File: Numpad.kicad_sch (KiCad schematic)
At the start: 102 parts, among them J1 USB_C_Receptacle_USB2.0, J3 AVR-ISP-6, Q101 DMN2041L, Q2 DMN2041L, SW10 SW_Push, SW11 SW_Push, SW12 SW_Push, SW13 SW_Push, SW14 SW_Push, SW15 SW_Push, SW16 SW_Push, SW17 SW_Push, SW18 SW_Push, SW19 SW_Push, SW2 SW_Push, SW21 SW_Push, SW3 SW_Push, SW4 SW_Push, SW5 SW_Push, SW6 SW_Push, SW7 SW_Push, SW8 SW_Push, SW9 SW_Push, U1 ATmega32U2-A, Y1 16MHz

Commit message: more routing
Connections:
- net D+: now also D1.3 (I/O2); no longer D1.2 (I/O1)
- net D-: now also D1.2 (I/O1); no longer D1.3 (I/O2)
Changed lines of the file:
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@@
   (junction (at 215.9 214.63) (diameter 0) (color 0 0 0 0)
   )
+  (junction (at 105.41 113.03) (diameter 0) (color 0 0 0 0)
+  )
   (junction (at 205.74 214.63) (diameter 0) (color 0 0 0 0)
   )
@@
   (junction (at 313.69 134.62) (diameter 0) (color 0 0 0 0)
   )
+  (junction (at 232.41 34.29) (diameter 0) (color 0 0 0 0)
+  )
+  (junction (at 182.88 196.85) (diameter 0) (color 0 0 0 0)
+  )
+  (junction (at 341.63 124.46) (diameter 0) (color 0 0 0 0)
+  )
+  (junction (at 177.8 93.98) (diameter 0) (color 0 0 0 0)
+  )
+  (junction (at 341.63 114.3) (diameter 0) (color 0 0 0 0)
+  )
+  (junction (at 195.58 229.87) (diameter 0) (color 0 0 0 0)
+  )
+  (junction (at 330.2 140.97) (diameter 0) (color 0 0 0 0)
+  )
+  (junction (at 215.9 229.87) (diameter 0) (color 0 0 0 0)
+  )
+  (junction (at 226.06 212.09) (diameter 0) (color 0 0 0 0)
+  )
+  (junction (at 205.74 212.09) (diameter 0) (color 0 0 0 0)
+  )
+  (junction (at 236.22 232.41) (diameter 0) (color 0 0 0 0)
+  )
+  (junction (at 185.42 196.85) (diameter 0) (color 0 0 0 0)
+  )
+  (junction (at 236.22 214.63) (diameter 0) (color 0 0 0 0)
+  )
+  (junction (at 242.57 34.29) (diameter 0) (color 0 0 0 0)
+  )
+  (junction (at 185.42 214.63) (diameter 0) (color 0 0 0 0)
+  )
+  (junction (at 355.6 139.7) (diameter 0) (color 0 0 0 0)
+  )
+  (junction (at 195.58 232.41) (diameter 0) (color 0 0 0 0)
+  )
+  (junction (at 344.17 130.81) (diameter 0) (color 0 0 0 0)
+  )
+  (junction (at 215.9 212.09) (diameter 0) (color 0 0 0 0)
+  )
+  (junction (at 316.23 130.81) (diameter 0) (color 0 0 0 0)
+  )
+  (junction (at 215.9 196.85) (diameter 0) (color 0 0 0 0)
+  )
+  (junction (at 345.44 151.13) (diameter 0) (color 0 0 0 0)
+  )
+  (junction (at 205.74 196.85) (diameter 0) (color 0 0 0 0)
+  )
+  (junction (at 226.06 214.63) (diameter 0) (color 0 0 0 0)
+  )
+  (junction (at 195.58 214.63) (diameter 0) (color 0 0 0 0)
+  )
+  (junction (at 237.49 34.29) (diameter 0) (color 0 0 0 0)
+  )
+  (junction (at 167.64 93.98) (diameter 0) (color 0 0 0 0)
+  )
+  (junction (at 182.88 214.63) (diameter 0) (color 0 0 0 0)
+  )
+  (junction (at 97.79 99.06) (diameter 0) (color 0 0 0 0)
+  )
+  (junction (at 355.6 114.3) (diameter 0) (color 0 0 0 0)
+  )
+  (junction (at 313.69 124.46) (diameter 0) (color 0 0 0 0)
+  )
+  (junction (at 313.69 114.3) (diameter 0) (color 0 0 0 0)
+  )
+  (junction (at 215.9 76.2) (diameter 0) (color 0 0 0 0)
+  )
+  (junction (at 205.74 229.87) (diameter 0) (color 0 0 0 0)
+  )
+  (junction (at 236.22 247.65) (diameter 0) (color 0 0 0 0)
+  )
+  (junction (at 226.06 232.41) (diameter 0) (color 0 0 0 0)
+  )
+  (junction (at 175.26 96.52) (diameter 0) (color 0 0 0 0)
+  )
+  (junction (at 177.8 88.9) (diameter 0) (color 0 0 0 0)
+  )
+  (junction (at 195.58 83.82) (diameter 0) (color 0 0 0 0)
+  )
+  (junction (at 96.52 113.03) (diameter 0) (color 0 0 0 0)
+  )
+  (junction (at 330.2 130.81) (diameter 0) (color 0 0 0 0)
+  )
+  (junction (at 215.9 147.32) (diameter 0) (color 0 0 0 0)
+  )
+  (junction (at 100.33 137.16) (diameter 0) (color 0 0 0 0)
+  )
+  (junction (at 330.2 120.65) (diameter 0) (color 0 0 0 0)
+  )
+  (junction (at 344.17 120.65) (diameter 0) (color 0 0 0 0)
+  )
+  (junction (at 205.74 232.41) (diameter 0) (color 0 0 0 0)
+  )
+  (junction (at 242.57 39.37) (diameter 0) (color 0 0 0 0)
+  )
+  (junction (at 327.66 114.3) (diameter 0) (color 0 0 0 0)
+  )
   (junction (at 104.14 113.03) (diameter 0) (color 0 0 0 0)
-  )
-  (junction (at 232.41 34.29) (diameter 0) (color 0 0 0 0)
-  )
-  (junction (at 182.88 196.85) (diameter 0) (color 0 0 0 0)
-  )
-  (junction (at 341.63 124.46) (diameter 0) (color 0 0 0 0)
-  )
-  (junction (at 177.8 93.98) (diameter 0) (color 0 0 0 0)
-  )
-  (junction (at 341.63 114.3) (diameter 0) (color 0 0 0 0)
-  )
-  (junction (at 195.58 229.87) (diameter 0) (color 0 0 0 0)
-  )
-  (junction (at 330.2 140.97) (diameter 0) (color 0 0 0 0)
-  )
-  (junction (at 215.9 229.87) (diameter 0) (color 0 0 0 0)
-  )
-  (junction (at 226.06 212.09) (diameter 0) (color 0 0 0 0)
-  )
-  (junction (at 205.74 212.09) (diameter 0) (color 0 0 0 0)
-  )
-  (junction (at 236.22 232.41) (diameter 0) (color 0 0 0 0)
-  )
-  (junction (at 185.42 196.85) (diameter 0) (color 0 0 0 0)
-  )
-  (junction (at 236.22 214.63) (diameter 0) (color 0 0 0 0)
-  )
-  (junction (at 242.57 34.29) (diameter 0) (color 0 0 0 0)
-  )
-  (junction (at 185.42 214.63) (diameter 0) (color 0 0 0 0)
-  )
-  (junction (at 355.6 139.7) (diameter 0) (color 0 0 0 0)
-  )
-  (junction (at 195.58 232.41) (diameter 0) (color 0 0 0 0)
-  )
-  (junction (at 344.17 130.81) (diameter 0) (color 0 0 0 0)
-  )
-  (junction (at 215.9 212.09) (diameter 0) (color 0 0 0 0)
-  )
-  (junction (at 316.23 130.81) (diameter 0) (color 0 0 0 0)
-  )
-  (junction (at 215.9 196.85) (diameter 0) (color 0 0 0 0)
-  )
-  (junction (at 345.44 151.13) (diameter 0) (color 0 0 0 0)
-  )
-  (junction (at 205.74 196.85) (diameter 0) (color 0 0 0 0)
-  )
-  (junction (at 226.06 214.63) (diameter 0) (color 0 0 0 0)
-  )
-  (junction (at 195.58 214.63) (diameter 0) (color 0 0 0 0)
-  )
-  (junction (at 237.49 34.29) (diameter 0) (color 0 0 0 0)
-  )
-  (junction (at 167.64 93.98) (diameter 0) (color 0 0 0 0)
-  )
-  (junction (at 105.41 118.11) (diameter 0) (color 0 0 0 0)
-  )
-  (junction (at 182.88 214.63) (diameter 0) (color 0 0 0 0)
-  )
-  (junction (at 97.79 99.06) (diameter 0) (color 0 0 0 0)
-  )
-  (junction (at 355.6 114.3) (diameter 0) (color 0 0 0 0)
-  )
-  (junction (at 313.69 124.46) (diameter 0) (color 0 0 0 0)
-  )
-  (junction (at 313.69 114.3) (diameter 0) (color 0 0 0 0)
-  )
-  (junction (at 215.9 76.2) (diameter 0) (color 0 0 0 0)
-  )
-  (junction (at 205.74 229.87) (diameter 0) (color 0 0 0 0)
-  )
-  (junction (at 236.22 247.65) (diameter 0) (color 0 0 0 0)
-  )
-  (junction (at 226.06 232.41) (diameter 0) (color 0 0 0 0)
-  )
-  (junction (at 175.26 96.52) (diameter 0) (color 0 0 0 0)
-  )
-  (junction (at 177.8 88.9) (diameter 0) (color 0 0 0 0)
-  )
-  (junction (at 195.58 83.82) (diameter 0) (color 0 0 0 0)
-  )
-  (junction (at 96.52 113.03) (diameter 0) (color 0 0 0 0)
-  )
-  (junction (at 330.2 130.81) (diameter 0) (color 0 0 0 0)
-  )
-  (junction (at 215.9 147.32) (diameter 0) (color 0 0 0 0)
-  )
-  (junction (at 100.33 137.16) (diameter 0) (color 0 0 0 0)
-  )
-  (junction (at 330.2 120.65) (diameter 0) (color 0 0 0 0)
-  )
-  (junction (at 344.17 120.65) (diameter 0) (color 0 0 0 0)
-  )
-  (junction (at 205.74 232.41) (diameter 0) (color 0 0 0 0)
-  )
-  (junction (at 242.57 39.37) (diameter 0) (color 0 0 0 0)
-  )
-  (junction (at 327.66 114.3) (diameter 0) (color 0 0 0 0)
   )
   (junction (at 341.63 144.78) (diameter 0) (color 0 0 0 0)
@@
     (stroke (width 0) (type default) (color 0 0 0 0))
   )
+  (wire (pts (xy 105.41 113.03) (xy 105.41 118.11))
+    (stroke (width 0) (type default) (color 0 0 0 0))
+  )
   (wire (pts (xy 226.06 228.6) (xy 226.06 229.87))
     (stroke (width 0) (type default) (color 0 0 0 0))
@@
     (stroke (width 0) (type default) (color 0 0 0 0))
   )
-  (wire (pts (xy 133.35 113.03) (xy 104.14 113.03))
+  (wire (pts (xy 133.35 124.46) (xy 133.35 113.03))
     (stroke (width 0) (type default) (color 0 0 0 0))
   )
@@
     (stroke (width 0) (type default) (color 0 0 0 0))
   )
-  (wire (pts (xy 105.41 124.46) (xy 105.41 118.11))
-    (stroke (width 0) (type default) (color 0 0 0 0))
-  )
   (wire (pts (xy 257.81 229.87) (xy 257.81 247.65))
     (stroke (width 0) (type default) (color 0 0 0 0))
@@
     (stroke (width 0) (type default) (color 0 0 0 0))
   )
-  (wire (pts (xy 133.35 124.46) (xy 133.35 113.03))
-    (stroke (width 0) (type default) (color 0 0 0 0))
-  )
   (wire (pts (xy 237.49 34.29) (xy 242.57 34.29))
     (stroke (width 0) (type default) (color 0 0 0 0))
@@
     (stroke (width 0) (type default) (color 0 0 0 0))
   )
+  (wire (pts (xy 133.35 113.03) (xy 105.41 113.03))
+    (stroke (width 0) (type default) (color 0 0 0 0))
+  )
   (wire (pts (xy 226.06 229.87) (xy 236.22 229.87))
     (stroke (width 0) (type default) (color 0 0 0 0))
@@
     (stroke (width 0) (type default) (color 0 0 0 0))
   )
-  (wire (pts (xy 106.68 124.46) (xy 105.41 124.46))
-    (stroke (width 0) (type default) (color 0 0 0 0))
-  )
   (wire (pts (xy 316.23 110.49) (xy 330.2 110.49))
     (stroke (width 0) (type default) (color 0 0 0 0))
@@
     (stroke (width 0) (type default) (color 0 0 0 0))
   )
+  (wire (pts (xy 132.08 124.46) (xy 133.35 124.46))
+    (stroke (width 0) (type default) (color 0 0 0 0))
+  )
   (wire (pts (xy 327.66 104.14) (xy 327.66 114.3))
     (stroke (width 0) (type default) (color 0 0 0 0))
@@
     (stroke (width 0) (type default) (color 0 0 0 0))
   )
+  (wire (pts (xy 104.14 124.46) (xy 104.14 113.03))
+    (stroke (width 0) (type default) (color 0 0 0 0))
+  )
   (wire (pts (xy 232.41 34.29) (xy 237.49 34.29))
     (stroke (width 0) (type default) (color 0 0 0 0))
   )
-  (wire (pts (xy 105.41 110.49) (xy 105.41 118.11))
+  (wire (pts (xy 105.41 110.49) (xy 105.41 113.03))
     (stroke (width 0) (type default) (color 0 0 0 0))
   )
@@
     (stroke (width 0) (type default) (color 0 0 0 0))
   )
+  (wire (pts (xy 106.68 124.46) (xy 104.14 124.46))
+    (stroke (width 0) (type default) (color 0 0 0 0))
+  )
   (wire (pts (xy 330.2 120.65) (xy 344.17 120.65))
     (stroke (width 0) (type default) (color 0 0 0 0))
@@
     (stroke (width 0) (type default) (color 0 0 0 0))
   )
-  (wire (pts (xy 132.08 124.46) (xy 133.35 124.46))
-    (stroke (width 0) (type default) (color 0 0 0 0))
-  )

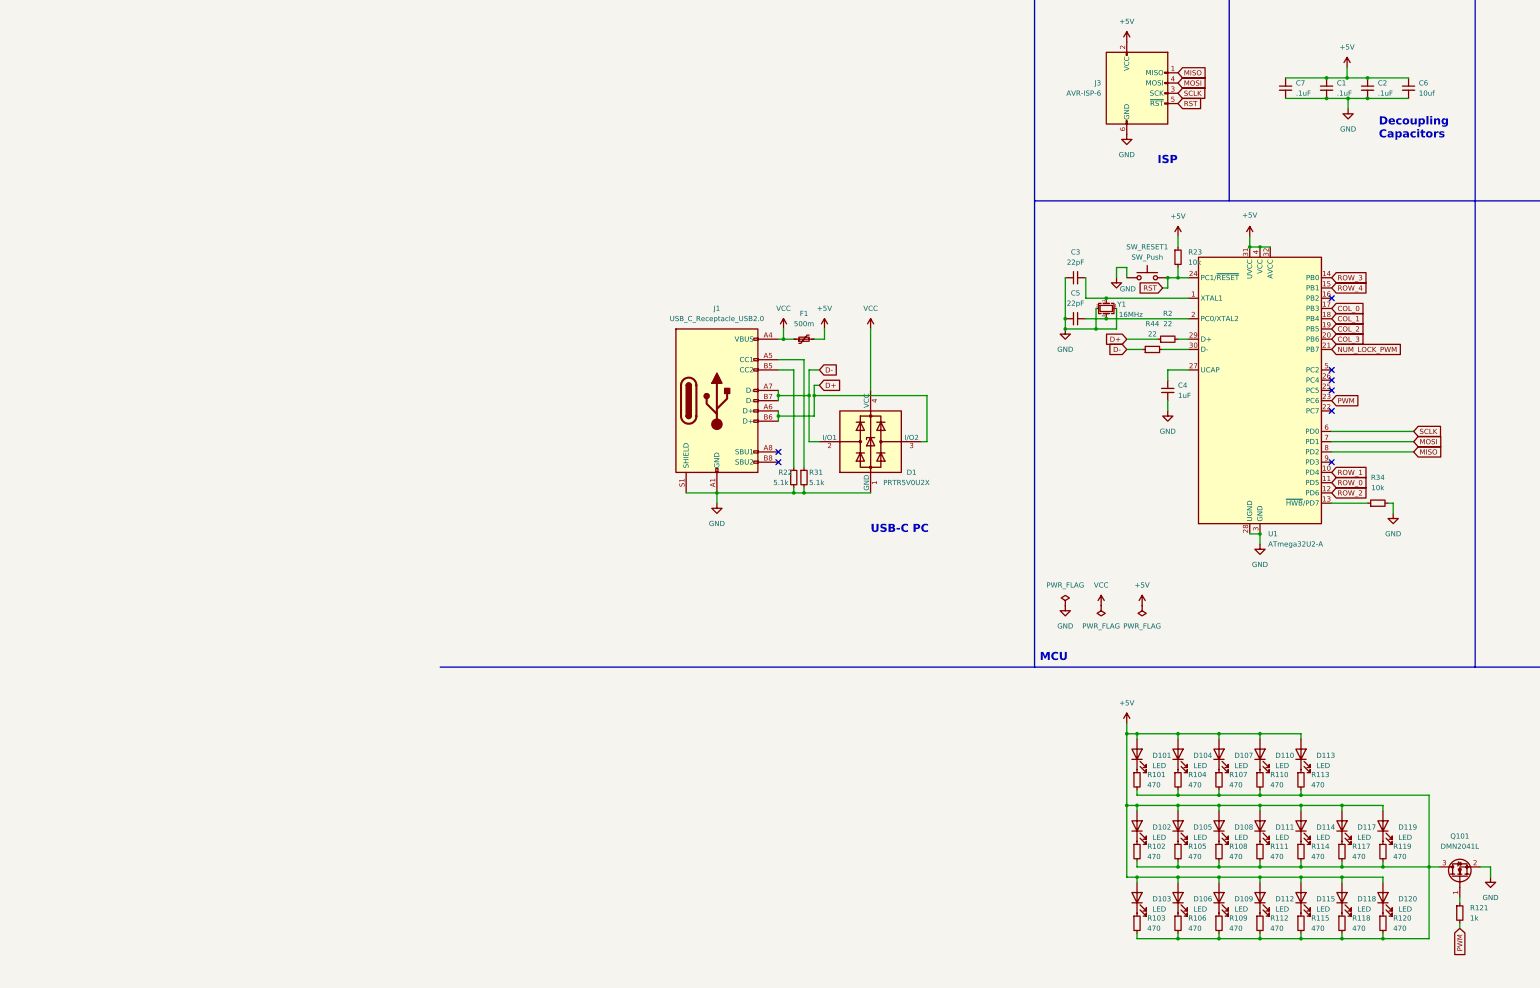
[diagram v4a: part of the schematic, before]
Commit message: swapped leds to rgb leds, and added a whole lot of routing
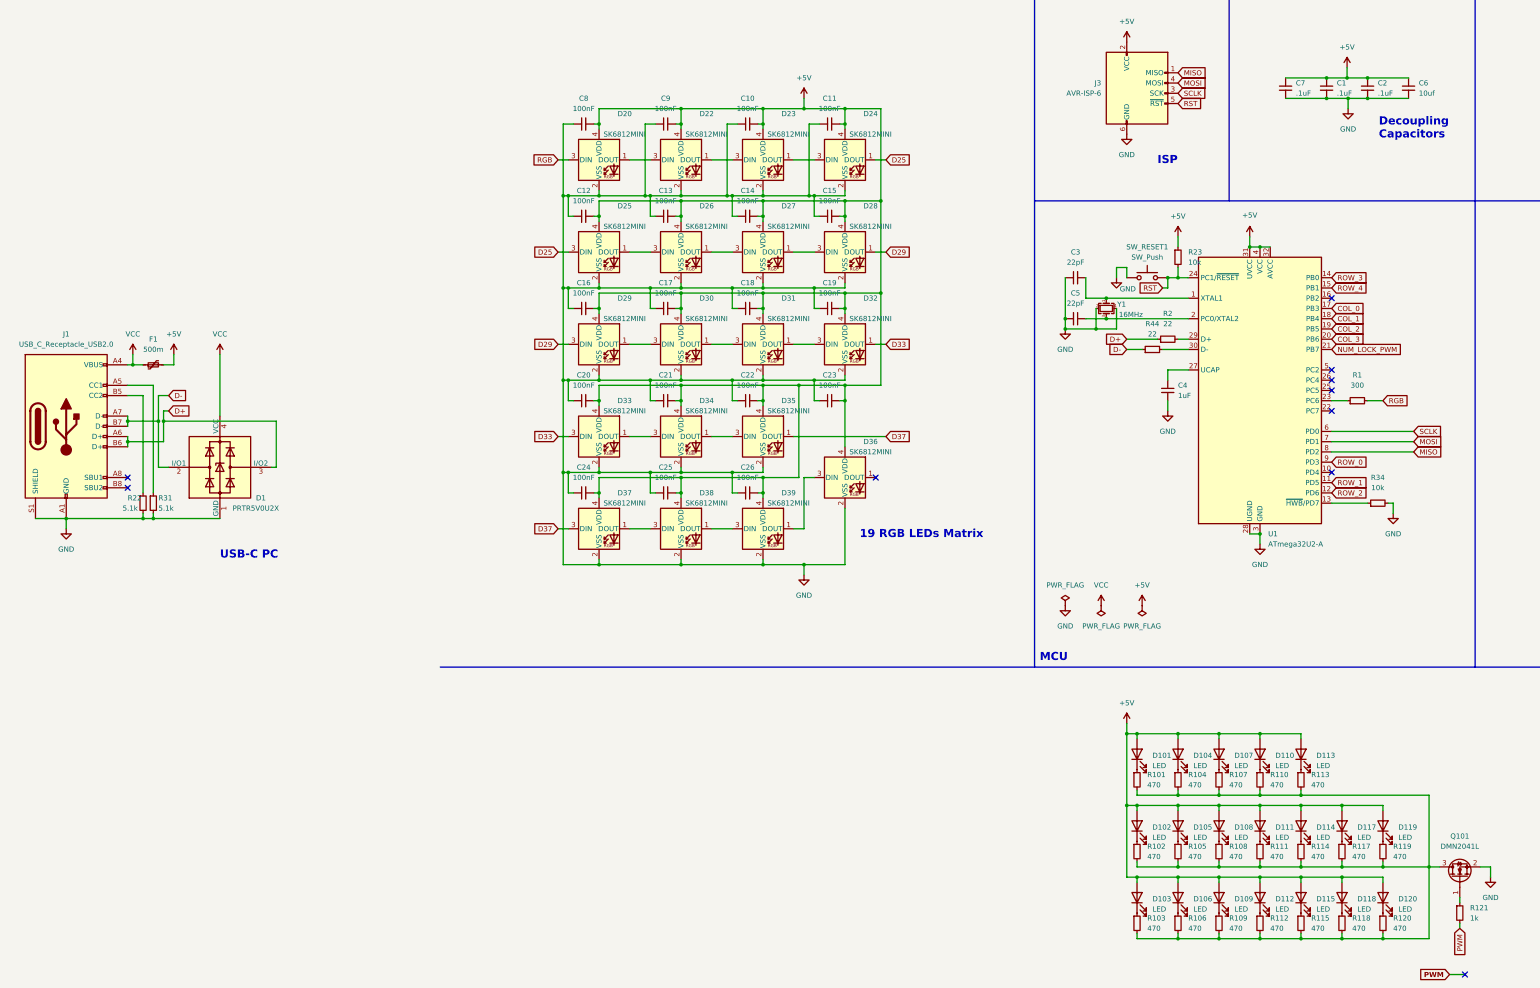
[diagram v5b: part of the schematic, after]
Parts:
- added C10, C11, C12, C13, C14, C15, C16, C17, C18, C19, C20, C21, C22, C23, C24, C25, C26, C8, C9: 100nF, Capacitor_SMD:C_0402_1005Metric, symbol Device:C_Small
- added D20, D22, D23, D24, D25, D26, D27, D28, D29, D30, D31, D32, D33, D34, D35, D36, D37, D38, D39: SK6812MINI, Keebio-Parts:SK6812-MINI-E, symbol LED:SK6812MINI
- added R1: 300, Resistor_SMD:R_0402_1005Metric, symbol Device:R_Small
- J3: footprint Keebio-Parts:ICSP_1.27mm -> Keebio-Parts:ICSP-Header
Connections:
- net +5V: now also C10.2, C11.2, C12.2, C13.2, C14.2, C15.2, C16.2, C17.2, C18.2, C19.2, C20.2, C21.2, C22.2, C23.2, C24.2, C25.2, C26.2, C8.2, C9.2, D20.4 (VDD), D22.4 (VDD), D23.4 (VDD), D24.4 (VDD), D25.4 (VDD), D26.4 (VDD), D27.4 (VDD), D28.4 (VDD), D29.4 (VDD), D30.4 (VDD), D31.4 (VDD), D32.4 (VDD), D33.4 (VDD), D34.4 (VDD), D35.4 (VDD), D36.4 (VDD), D37.4 (VDD), D38.4 (VDD), D39.4 (VDD)
- net GND: now also C10.1, C11.1, C12.1, C13.1, C14.1, C15.1, C16.1, C17.1, C18.1, C19.1, C20.1, C21.1, C22.1, C23.1, C24.1, C25.1, C26.1, C8.1, C9.1, D20.2 (VSS), D22.2 (VSS), D23.2 (VSS), D24.2 (VSS), D25.2 (VSS), D26.2 (VSS), D27.2 (VSS), D28.2 (VSS), D29.2 (VSS), D30.2 (VSS), D31.2 (VSS), D32.2 (VSS), D33.2 (VSS), D34.2 (VSS), D35.2 (VSS), D36.2 (VSS), D37.2 (VSS), D38.2 (VSS), D39.2 (VSS)
- net PWM: no longer U1.23 (PC6)
- net ROW_0: now also U1.9 (PD3); no longer U1.11 (PD5)
- net ROW_1: now also U1.11 (PD5); no longer U1.10 (PD4)
- new net: D25.1 (DOUT), D26.3 (DIN)
- new net: D23.1 (DOUT), D24.3 (DIN)
- new net: D22.1 (DOUT), D23.3 (DIN)
- new net: D31.1 (DOUT), D32.3 (DIN)
- new net: D36.3 (DIN), D39.1 (DOUT)
- new net: D38.1 (DOUT), D39.3 (DIN)
- new net: D30.1 (DOUT), D31.3 (DIN)
- new net: D29.1 (DOUT), D30.3 (DIN)
- new net: D20.1 (DOUT), D22.3 (DIN)
- new net: D34.1 (DOUT), D35.3 (DIN)
- new net: D33.1 (DOUT), D34.3 (DIN)
- new net: D27.1 (DOUT), D28.3 (DIN)
- new net: D26.1 (DOUT), D27.3 (DIN)
- new net: R1.1, U1.23 (PC6)
- new net: D37.1 (DOUT), D38.3 (DIN)
- new net D25: D24.1 (DOUT), D25.3 (DIN)
- new net D29: D28.1 (DOUT), D29.3 (DIN)
- new net D33: D32.1 (DOUT), D33.3 (DIN)
- new net D37: D35.1 (DOUT), D37.3 (DIN)
- new net RGB: D20.3 (DIN), R1.2
- no-connect marks 8 -> 10
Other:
- note added: "19 RGB LEDs Matrix"
- moved on the sheet: D1, F1, J1, R22, R31

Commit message: some more routing and messing around with usb rcep
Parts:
- removed D101, D102, D103, D104, D105, D106, D107, D108, D109, D110, D111, D112, D113, D114, D115, D117, D118, D119, D120: LED, LED_SMD:LED_PLCC_2835, symbol Device:LED
- removed Q101: DMN2041L, Package_TO_SOT_SMD:SOT-23, symbol Transistor_FET:DMN2041L
- removed R101, R102, R103, R104, R105, R106, R107, R108, R109, R110, R111, R112, R113, R114, R115, R117, R118, R119, R120: 470, Resistor_SMD:R_0402_1005Metric, symbol Device:R_Small
- removed R121: 1k, Resistor_SMD:R_0402_1005Metric, symbol Device:R_Small
- added H1, H2, H3, H4: MountingHole, MountingHole:MountingHole_2.2mm_M2_DIN965_Pad, symbol Mechanical:MountingHole
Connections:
- no-connect marks 10 -> 9
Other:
- note removed: "19 LEDs"
- moved on the sheet: D1, F1, J1, R22, R31
